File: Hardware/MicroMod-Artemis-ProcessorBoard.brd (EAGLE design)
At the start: 22 x 22 mm, 42 parts, among them J1 MICROMOD-2222, U1 ARTEMIS_MODULESMD, U2 TSV524, U6 CH340E_MSOP10, Y1 32.768kHz

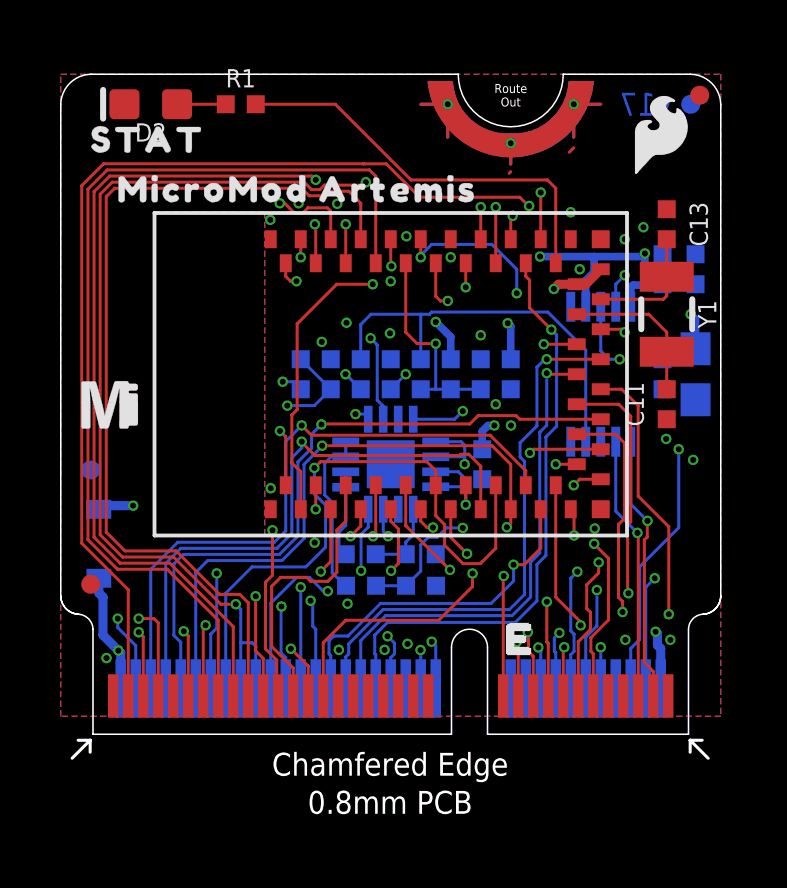
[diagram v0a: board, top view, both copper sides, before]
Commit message: add smd jumper between artemis and STAT_LED current limiting resistor
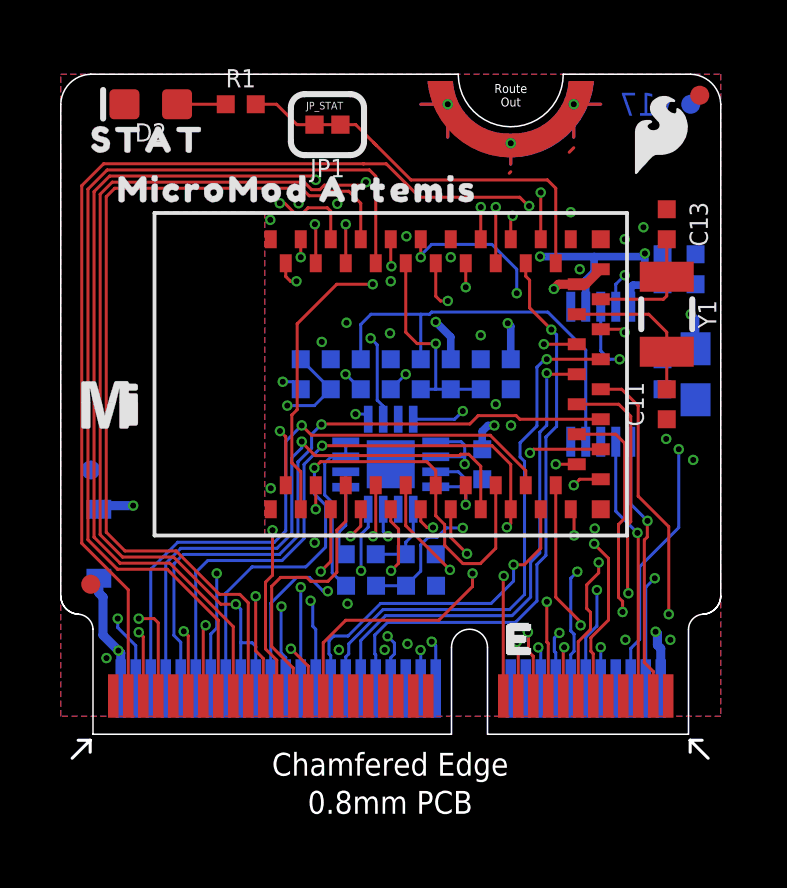
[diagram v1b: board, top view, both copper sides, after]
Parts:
- added JP1: JUMPER-SMT_2_NC_TRACE_SILK, SparkFun-Jumpers:SMT-JUMPER_2_NC_TRACE_SILK
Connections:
- new net N$1: JP1.2, R1.2
- net LED_BUILTIN: now also JP1.1; no longer R1.2
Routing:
- net LED_BUILTIN: track 13.7 -> 10.7 mm
- net N$1: track 0.00 -> 2.24 mm
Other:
- board text added: "JP_STAT"
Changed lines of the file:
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@@
 <drawing>
 <settings>
-<setting alwaysvectorfont="yes"/>
+<setting alwaysvectorfont="no"/>
 <setting verticaltext="up"/>
 </settings>
-<grid distance="0.05" unitdist="inch" unit="inch" style="lines" multiple="1" display="yes" altdistance="0.005" altunitdist="inch" altunit="inch"/>
+<grid distance="0.001" unitdist="inch" unit="mil" style="lines" multiple="1" display="yes" altdistance="0.005" altunitdist="inch" altunit="inch"/>
 <layers>
 <layer number="1" name="Top" color="4" fill="1" visible="yes" active="yes"/>
@@
 <layer number="20" name="Dimension" color="24" fill="1" visible="yes" active="yes"/>
 <layer number="21" name="tPlace" color="16" fill="1" visible="yes" active="yes"/>
-<layer number="22" name="bPlace" color="14" fill="1" visible="yes" active="yes"/>
+<layer number="22" name="bPlace" color="14" fill="1" visible="no" active="yes"/>
 <layer number="23" name="tOrigins" color="15" fill="1" visible="yes" active="yes"/>
 <layer number="24" name="bOrigins" color="15" fill="1" visible="yes" active="yes"/>
@@
 <text x="17.78" y="-8.89" size="1.778" layer="51" font="vector" ratio="15">N. Seidle</text>
 <wire x1="13.25" y1="22" x2="16.75" y2="22" width="0.05" layer="20" curve="180"/>
+<text x="8.1788" y="20.828" size="0.254" layer="21">JP_STAT</text>
 </plain>
 <attributes>
@@
 <element name="U$9" library="output" package="ARTEMIS0" value="" x="13.97" y="13.716" smashed="yes" rot="MR0"/>
 <element name="U$11" library="output" package="STAT0" value="" x="0.381" y="19.812" smashed="yes"/>
+<element name="JP1" library="SparkFun-Jumpers" package="SMT-JUMPER_2_NC_TRACE_SILK" package3d_urn="urn:adsk.eagle:package:39281/1" value="JUMPER-SMT_2_NC_TRACE_SILK" x="8.89" y="20.32" smashed="yes" rot="R180">
+<attribute name="NAME" x="8.89" y="19.177" size="0.6096" layer="25" font="vector" ratio="20" rot="R180" align="bottom-center"/>
+<attribute name="VALUE" x="8.89" y="21.463" size="0.6096" layer="27" font="vector" ratio="20" rot="R180" align="top-center"/>
+</element>
 </elements>
 <signals>
@@
 <signal name="LED_BUILTIN">
 <contactref element="U1" pad="~D19"/>
-<contactref element="R1" pad="2"/>
-<wire x1="9.15208125" y1="21" x2="6.5" y2="21" width="0.1016" layer="1"/>
-<wire x1="11.676040625" y1="18.476040625" x2="9.15208125" y2="21" width="0.1016" layer="1"/>
+<wire x1="11.676040625" y1="18.476040625" x2="10.504040625" y2="19.648040625" width="0.1016" layer="1"/>
+<wire x1="10.504040625" y1="19.648040625" x2="10.42208125" y2="19.73" width="0.1016" layer="1"/>
 <wire x1="16.223959375" y1="18.476040625" x2="11.676040625" y2="18.476040625" width="0.1016" layer="1"/>
 <wire x1="16.5" y1="15.7" x2="16.5" y2="18.2" width="0.1016" layer="1"/>
 <wire x1="16.5" y1="18.2" x2="16.223959375" y2="18.476040625" width="0.1016" layer="1"/>
+<contactref element="JP1" pad="1"/>
+<wire x1="10.504040625" y1="19.648040625" x2="9.83208125" y2="20.32" width="0.1016" layer="1"/>
+<wire x1="9.83208125" y1="20.32" x2="9.3218" y2="20.32" width="0.1016" layer="1"/>
 </signal>
 <signal name="SCL1">
@@
 <wire x1="17.78" y1="15.407525" x2="17.78" y2="15.9222" width="0.254" layer="16"/>
 </signal>
+<signal name="N$1">
+<contactref element="R1" pad="2"/>
+<contactref element="JP1" pad="2"/>
+<wire x1="8.4582" y1="20.32" x2="7.874" y2="20.32" width="0.1016" layer="1"/>
+<wire x1="7.194" y1="21" x2="6.5" y2="21" width="0.1016" layer="1"/>
+<wire x1="7.874" y1="20.32" x2="7.194" y2="21" width="0.1016" layer="1"/>
+</signal>
 </signals>
 <mfgpreviewcolors>
@@
 which will not be processed correctly with this version.
 </note>
+<note version="8.3" severity="warning">
+Since Version 8.3, EAGLE supports URNs for individual library
+assets (packages, symbols, and devices). The URNs of those assets
+will not be understood (or retained) with this version.
+</note>
+<note version="8.3" severity="warning">
+Since Version 8.3, EAGLE supports the association of 3D packages
+with devices in libraries, schematics, and board files. Those 3D
+packages will not be understood (or retained) with this version.
+</note>
 </compatibility>
